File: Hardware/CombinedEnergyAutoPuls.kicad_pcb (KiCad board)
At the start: 2 copper layers, 0 parts

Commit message: STAGE: Component placed on PCB
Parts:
- added A1: Arduino_Ethernet, Local_MCU_Module_Library:Arduino_Ethernet_WithMountingHoles, F.Cu at (33.0, 2.54)
- added C1: C330nf, Capacitor_SMD:C_0805_2012Metric, F.Cu at (55.9, 62.2)
- added C2: C10uf, Capacitor_SMD:C_0603_1608Metric, F.Cu at (20.3, 63.5)
- added C3: C100nf, Capacitor_SMD:C_0402_1005Metric, F.Cu at (71.1, 61.0)
- added D1: 1N4148WS, Diode_SMD:D_SOD-323F, F.Cu at (55.9, 7.62)
- added D10: D_Z2V7, Diode_THT:D_DO-34_SOD68_P7.62mm_Horizontal, F.Cu at (68.6, 50.8)
- added D11: 1N4004, Diode_THT:D_DO-41_SOD81_P12.70mm_Horizontal, F.Cu at (55.9, 55.9)
- added D2: 1N4148WS, Diode_SMD:D_SOD-323F, F.Cu at (53.3, 7.62)
- added D3: 1N4148WS, Diode_SMD:D_SOD-323F, F.Cu at (50.8, 7.62)
- added D4: 1N4148WS, Diode_SMD:D_SOD-323F, F.Cu at (41.9, 44.5)
- added D5: 1N4148WS, Diode_SMD:D_SOD-323F, F.Cu at (45.7, 44.5)
- added D6: 1N4148WS, Diode_SMD:D_SOD-323F, F.Cu at (48.3, 44.5)
- added D7: 1N4148WS, Diode_SMD:D_SOD-323F, F.Cu at (50.8, 44.5)
- added D8: 1N4148WS, Diode_SMD:D_SOD-323F, F.Cu at (55.9, 44.5)
- added D9: LED_G3, LED_THT:LED_D3.0mm, F.Cu at (39.4, 57.3)
- added J1: Screw_Terminal_01x04, Local_Connectors:TerminalBlock_PT-1,5-4-5.0-H_1x04_P5.00mm_Horizontal-(F.Mount), F.Cu at (77.7, 41.0)
- added J2: Screw_Terminal_01x04, Local_Connectors:TerminalBlock_PT-1,5-4-5.0-H_1x04_P5.00mm_Horizontal-(F.Mount), F.Cu at (77.7, 20.7)
- added J3: Arduino_USB-Serial_Card, Local_Connectors:Arduino_USB-Serial_Card, F.Cu at (102.9, 2.54)
- added J4: Arduino_USB-Serial_Card_Connector, Local_Connectors:Arduino_USB-Serial_Card_EdgeConn, F.Cu at (34.6, 62.0)
- added J5: AudioJack3_Switch, Local_Connectors:AUDIO_JACK_ASJ-195-L-HT-(F.Mount), F.Cu at (0.10, 55.5)
- added J6: Screw_Terminal_01x04, Local_Connectors:TerminalBlock_PT-1,5-4-5.0-H_1x04_P5.00mm_Horizontal-(F.Mount), F.Cu at (77.7, 61.3)
- added JP1: Jumper_3_Bridged12, Connector_PinHeader_2.54mm:PinHeader_1x03_P2.54mm_Vertical, F.Cu at (15.2, 57.0)
- added Q1: S8550_PNP, Package_TO_SOT_SMD:SOT-23, F.Cu at (59.7, 14.0)
- added Q2: S8050_NPN, Package_TO_SOT_SMD:SOT-23, F.Cu at (62.2, 24.1)
- added Q3: S8050_NPN, Package_TO_SOT_SMD:SOT-23, F.Cu at (25.4, 62.2)
- added R1: R10K, Resistor_SMD:R_0402_1005Metric, F.Cu at (53.3, 15.2)
- added R2: R680K, Resistor_SMD:R_0603_1608Metric, F.Cu at (53.3, 12.7)
- added R3: R39K, Resistor_SMD:R_0402_1005Metric, F.Cu at (67.3, 24.9)
- added R4: R180K, Resistor_SMD:R_0603_1608Metric, F.Cu at (62.2, 19.1)
- added R5: R180K, Resistor_SMD:R_0603_1608Metric, F.Cu at (58.4, 7.62)
- added R6: R220, Resistor_SMD:R_0805_2012Metric, F.Cu at (49.5, 54.6)
- added R7: R56, Resistor_SMD:R_1206_3216Metric, F.Cu at (20.3, 59.7)
- added R8: R10K, Resistor_SMD:R_0402_1005Metric, F.Cu at (19.1, 55.9)
- added R9: R10K, Resistor_SMD:R_0402_1005Metric, F.Cu at (24.1, 55.9)
- added U1: L78S05CV, Package_TO_SOT_THT:TO-220-3_Vertical, F.Cu at (66.0, 61.3)
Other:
- board outline added: 113.8 x 67 mm

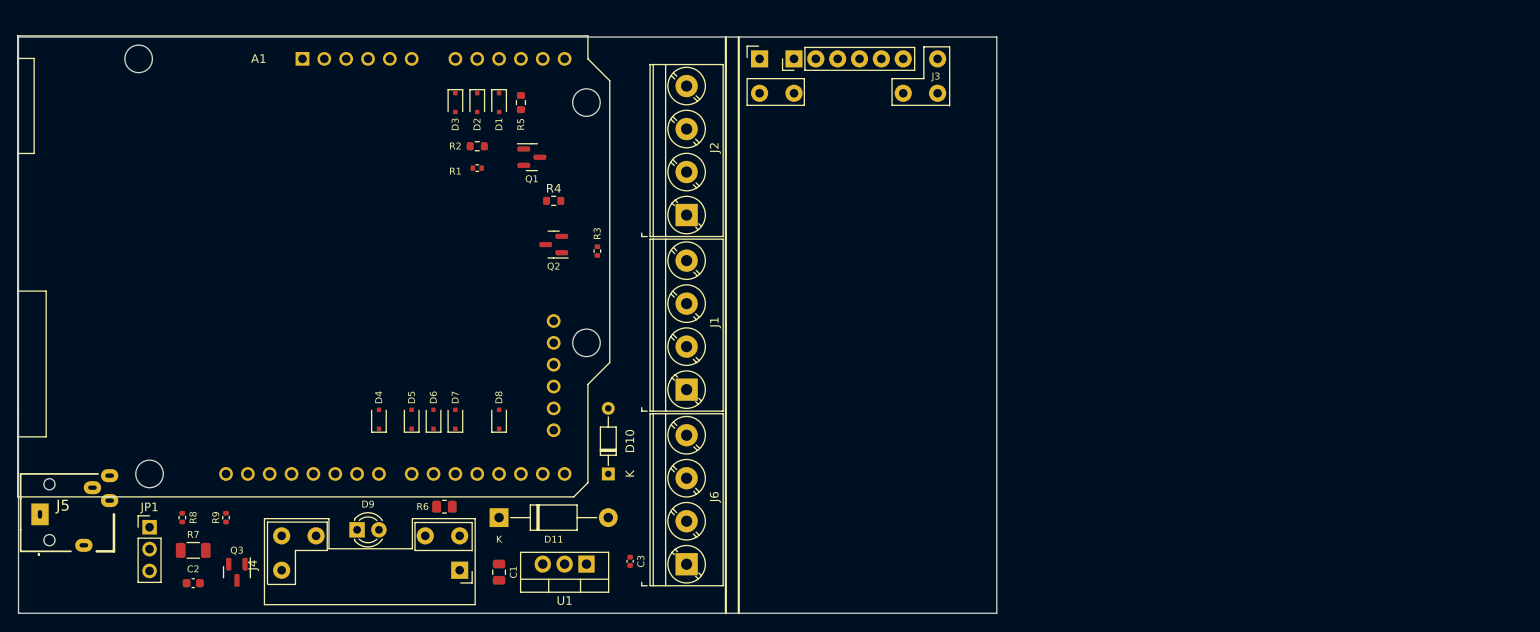
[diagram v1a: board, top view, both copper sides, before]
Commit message: Schematics and components placed on BCB for autoStart added to the project.
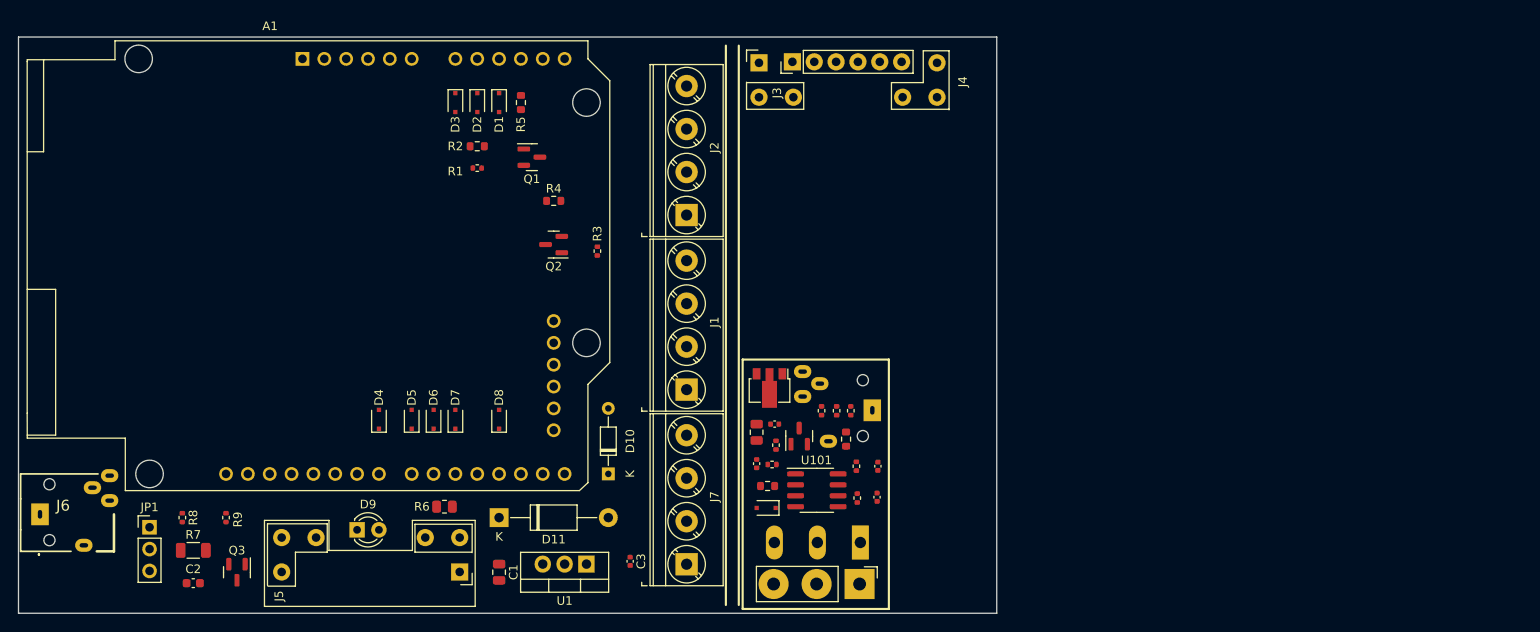
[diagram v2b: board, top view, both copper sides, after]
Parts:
- added C101: C10nf, Capacitor_SMD:C_0402_1005Metric, F.Cu at (99.9, 49.9)
- added C102: C100nf, Capacitor_SMD:C_0402_1005Metric, F.Cu at (99.8, 53.5)
- added C103: C100nf, Capacitor_SMD:C_0402_1005Metric, F.Cu at (85.8, 49.6)
- added C104: C100nf, Capacitor_SMD:C_0402_1005Metric, F.Cu at (87.9, 45.0)
- added C105: C330nf, Capacitor_SMD:C_0805_2012Metric, F.Cu at (85.8, 46.0)
- added D101: 1N4148WS, Diode_SMD:D_SOD-323F, F.Cu at (86.9, 54.8)
- added J101: AudioJack3_Switch, Local_Connectors:AUDIO_JACK_ASJ-195-L-HT-(B.Mount), F.Cu at (101.7, 43.4)
- added J102: Screw_Terminal_01x03, Local_Connectors:Phoenix_TERM_BLOCK_3POS_45DEG_5MM_PCB-(B.Mount), F.Cu at (97.9, 58.8)
- added J103: Conn_3P, Local_Connectors:PinHeader_1x03_P_5mm_Vertical-(F.Mount), F.Cu at (97.8, 63.6)
- added J5: Arduino_USB-Serial_Card_Connector, Local_Connectors:Arduino_USB-Serial_Card_EdgeConn, F.Cu at (34.6, 62.2)
- added Q101: S8050, Package_TO_SOT_SMD:SOT-23, F.Cu at (90.8, 46.4)
- added R101: R10K, Resistor_SMD:R_0402_1005Metric, F.Cu at (96.8, 43.5)
- added R102: R10K, Resistor_SMD:R_0402_1005Metric, F.Cu at (95.1, 43.5)
- added R103: R10K, Resistor_SMD:R_0402_1005Metric, F.Cu at (93.4, 43.5)
- added R104: R330K, Resistor_SMD:R_0402_1005Metric, F.Cu at (97.4, 49.9)
- added R105: R100K, Resistor_SMD:R_0402_1005Metric, F.Cu at (97.5, 53.6)
- added R106: R680K, Resistor_SMD:R_0603_1608Metric, F.Cu at (87.1, 52.2)
- added R107: R150K, Resistor_SMD:R_0402_1005Metric, F.Cu at (88.1, 47.5)
- added R108: R33K, Resistor_SMD:R_0402_1005Metric, F.Cu at (87.6, 49.7)
- added R109: R180K, Resistor_SMD:R_0603_1608Metric, F.Cu at (96.2, 46.8)
- added U101: LM358DR2G, Package_SO:SOIC-8_3.9x4.9mm_P1.27mm, F.Cu at (92.8, 52.7)
- added U102: 78L05, Package_TO_SOT_SMD:SOT-89-3, F.Cu at (87.3, 40.8)
- J3: value Arduino_USB-Serial_Card -> Pin_Header_1x6; footprint Local_Connectors:Arduino_USB-Serial_Card -> Local_Connectors:PinHeader_1x06_P_0,1in_Vertical
- J4: value Arduino_USB-Serial_Card_Connector -> Arduino_USB-Serial_Card; footprint Local_Connectors:Arduino_USB-Serial_Card_EdgeConn -> Local_Connectors:Arduino_USB-Serial_Card
- moved J4 78.3 mm to (86.1, 3.00), turned to -90 degrees
- moved J3 12.9 mm to (90.0, 2.88), turned to 90 degrees
- renumbered J5 to J6, J6 to J7
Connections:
- J3 pad 1: unconnected-(J3-Pad1) -> GND3
- J3 pad 2: unconnected-(J3-Pad2) -> Net-(J3-Pad2)
- J3 pad 3: unconnected-(J3-Pad3) -> VCC1
- J3 pad 4: unconnected-(J3-Pad4) -> Net-(J3-Pad4)
- J3 pad 5: unconnected-(J3-Pad5) -> Net-(J3-Pad5)
- J3 pad 6: unconnected-(J3-Pad6) -> Net-(J3-Pad6)
- J4 pad 1: GND -> GND3
- J4 pad 2: Net-(A1-Pad30) -> Net-(J3-Pad2)
- J4 pad 3: VCC -> VCC1
- J4 pad 4: Net-(A1-Pad32) -> Net-(J3-Pad4)
- J4 pad 5: Net-(A1-Pad33) -> Net-(J3-Pad5)
- J4 pad 6: Net-(A1-Pad34) -> Net-(J3-Pad6)

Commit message: UPD: - Schematics and components placed on BCB for ProgrameablePulseGenerator added to the project
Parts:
- added A201: Arduino_Nano_v3, Module:Arduino_Nano, F.Cu at (122.7, 43.0)
- added AE201: Antenna, Local_Misckllaneous_Library:Undefined_Antenna(B.Mount), F.Cu at (111.8, 4.45)
- added C201: C100nf, Capacitor_SMD:C_0402_1005Metric, F.Cu at (129.5, 63.0)
- added C202: C330nf, Capacitor_SMD:C_0805_2012Metric, F.Cu at (129.5, 58.4)
- added D201: 1N4148WS, Diode_SMD:D_SOD-323F, F.Cu at (163.2, 50.8)
- added D202: LED, LED_SMD:LED_0805_2012Metric, F.Cu at (128.8, 53.3)
- added D203: 1N4148WS, Diode_SMD:D_SOD-323F, F.Cu at (163.2, 45.7)
- added D204: LED, LED_SMD:LED_0805_2012Metric, F.Cu at (128.6, 48.3)
- added D205: 1N4148WS, Diode_SMD:D_SOD-323F, F.Cu at (163.2, 40.6)
- added D206: LED, LED_SMD:LED_0805_2012Metric, F.Cu at (128.6, 43.2)
- added D207: 1N4148WS, Diode_SMD:D_SOD-323F, F.Cu at (163.2, 35.6)
- added D208: LED, LED_SMD:LED_0805_2012Metric, F.Cu at (128.6, 38.1)
- added D209: 1N4148WS, Diode_SMD:D_SOD-323F, F.Cu at (163.2, 30.5)
- added D210: LED, LED_SMD:LED_0805_2012Metric, F.Cu at (128.6, 33.0)
- added D211: 1N4148WS, Diode_SMD:D_SOD-323F, F.Cu at (163.2, 25.4)
- added D212: LED, LED_SMD:LED_0805_2012Metric, F.Cu at (128.6, 27.9)
- added D213: 1N4148WS, Diode_SMD:D_SOD-323F, F.Cu at (163.2, 20.3)
- added D214: LED, LED_SMD:LED_0805_2012Metric, F.Cu at (128.8, 22.9)
- added D215: 1N4148WS, Diode_SMD:D_SOD-323F, F.Cu at (163.2, 15.2)
- added D216: LED, LED_SMD:LED_0805_2012Metric, F.Cu at (128.8, 17.8)
- added D217: 1N4148WS, Diode_SMD:D_SOD-323F, F.Cu at (163.2, 10.2)
- added D218: LED, LED_SMD:LED_0805_2012Metric, F.Cu at (128.8, 12.7)
- added D219: 1N4148WS, Diode_SMD:D_SOD-323F, F.Cu at (163.2, 5.08)
- added D220: LED, LED_SMD:LED_0805_2012Metric, F.Cu at (128.8, 7.62)
- added J201: Conn_20P_Female, Connector_PinHeader_2.54mm:PinHeader_1x20_P2.54mm_Vertical, F.Cu at (142.2, 53.3)
- added J202: Conn_20P_Female, Connector_PinHeader_2.54mm:PinHeader_1x20_P2.54mm_Vertical, F.Cu at (170.2, 53.3)
- added J203: Conn_4P_Female, Connector_PinHeader_2.54mm:PinHeader_1x04_P2.54mm_Vertical, F.Cu at (170.2, 63.5)
- added J204: Conn_4P_Female, Connector_PinHeader_2.54mm:PinHeader_1x04_P2.54mm_Vertical, F.Cu at (152.4, 63.5)
- added J205: Barrel_Jack_Switch, Local_Connectors:BarrelJack_Horizontal(F.Mount), F.Cu at (110.2, 52.4)
- added JP201: SolderJumper, Local_Connectors:SolderJumper-2_P1.3mm_Bridged_RoundedPad1.0x1.5mm(B.Mount), F.Cu at (163.2, 50.8)
- added JP202: SolderJumper, Local_Connectors:SolderJumper-2_P1.3mm_Bridged_RoundedPad1.0x1.5mm(B.Mount), F.Cu at (163.2, 45.7)
- added JP203: SolderJumper, Local_Connectors:SolderJumper-2_P1.3mm_Bridged_RoundedPad1.0x1.5mm(B.Mount), F.Cu at (163.2, 40.6)
- added JP204: SolderJumper, Local_Connectors:SolderJumper-2_P1.3mm_Bridged_RoundedPad1.0x1.5mm(B.Mount), F.Cu at (163.2, 35.6)
- added JP205: SolderJumper, Local_Connectors:SolderJumper-2_P1.3mm_Bridged_RoundedPad1.0x1.5mm(B.Mount), F.Cu at (163.2, 30.5)
- added JP206: SolderJumper, Local_Connectors:SolderJumper-2_P1.3mm_Bridged_RoundedPad1.0x1.5mm(B.Mount), F.Cu at (163.2, 25.4)
- added JP207: SolderJumper, Local_Connectors:SolderJumper-2_P1.3mm_Bridged_RoundedPad1.0x1.5mm(B.Mount), F.Cu at (163.2, 20.3)
- added JP208: SolderJumper, Local_Connectors:SolderJumper-2_P1.3mm_Bridged_RoundedPad1.0x1.5mm(B.Mount), F.Cu at (163.2, 15.2)
- added JP209: SolderJumper, Local_Connectors:SolderJumper-2_P1.3mm_Bridged_RoundedPad1.0x1.5mm(B.Mount), F.Cu at (163.2, 10.2)
- added JP210: SolderJumper, Local_Connectors:SolderJumper-2_P1.3mm_Bridged_RoundedPad1.0x1.5mm(B.Mount), F.Cu at (163.2, 5.08)
- added JP211: Jumper_3_Bridged12, Connector_PinHeader_2.54mm:PinHeader_1x03_P2.54mm_Vertical, F.Cu at (134.6, 58.4)
- added R201: R390, Resistor_SMD:R_0603_1608Metric, F.Cu at (135.5, 50.8)
- added R202: R180, Resistor_SMD:R_0805_2012Metric, F.Cu at (135.5, 53.3)
- added R203: R390, Resistor_SMD:R_0603_1608Metric, F.Cu at (135.4, 45.7)
- added R204: R180, Resistor_SMD:R_0805_2012Metric, F.Cu at (135.5, 48.3)
- added R205: R390, Resistor_SMD:R_0603_1608Metric, F.Cu at (135.4, 40.6)
- added R206: R180, Resistor_SMD:R_0805_2012Metric, F.Cu at (135.4, 43.2)
- added R207: R390, Resistor_SMD:R_0603_1608Metric, F.Cu at (135.4, 35.6)
- added R208: R180, Resistor_SMD:R_0805_2012Metric, F.Cu at (135.5, 38.1)
- added R209: R390, Resistor_SMD:R_0603_1608Metric, F.Cu at (135.4, 30.5)
- added R210: R180, Resistor_SMD:R_0805_2012Metric, F.Cu at (135.5, 33.0)
- added R211: R390, Resistor_SMD:R_0603_1608Metric, F.Cu at (135.4, 25.4)
- added R212: R180, Resistor_SMD:R_0805_2012Metric, F.Cu at (135.5, 27.9)
- added R213: R390, Resistor_SMD:R_0603_1608Metric, F.Cu at (135.4, 20.3)
- added R214: R180, Resistor_SMD:R_0805_2012Metric, F.Cu at (135.4, 22.9)
- added R215: R390, Resistor_SMD:R_0603_1608Metric, F.Cu at (135.5, 15.2)
- added R216: R180, Resistor_SMD:R_0805_2012Metric, F.Cu at (135.5, 17.8)
- added R217: R390, Resistor_SMD:R_0603_1608Metric, F.Cu at (135.5, 10.2)
- added R218: R180, Resistor_SMD:R_0805_2012Metric, F.Cu at (135.5, 12.7)
- added R219: R390, Resistor_SMD:R_0603_1608Metric, F.Cu at (135.4, 5.08)
- added R220: R180, Resistor_SMD:R_0805_2012Metric, F.Cu at (135.5, 7.62)
- added R221: R390, Resistor_SMD:R_0603_1608Metric, F.Cu at (144.8, 57.1)
- added SW201: THT_SW_4_Tactile, Local_Misckllaneous_Library:THT_SW_Tactile(F.Mount), F.Cu at (118.3, 58.7)
- added U201: PC817, Local_Misckllaneous_Library:DIP-4_W7.62mm_Slim(F.Mount), F.Cu at (148.6, 50.8)
- added U202: PC817, Local_Misckllaneous_Library:DIP-4_W7.62mm_Slim(F.Mount), F.Cu at (148.6, 45.7)
- added U203: PC817, Local_Misckllaneous_Library:DIP-4_W7.62mm_Slim(F.Mount), F.Cu at (148.6, 40.6)
- added U204: PC817, Local_Misckllaneous_Library:DIP-4_W7.62mm_Slim(F.Mount), F.Cu at (148.6, 35.6)
- added U205: PC817, Local_Misckllaneous_Library:DIP-4_W7.62mm_Slim(F.Mount), F.Cu at (148.6, 30.5)
- added U206: PC817, Local_Misckllaneous_Library:DIP-4_W7.62mm_Slim(F.Mount), F.Cu at (148.6, 25.4)
- added U207: PC817, Local_Misckllaneous_Library:DIP-4_W7.62mm_Slim(F.Mount), F.Cu at (148.6, 20.3)
- added U208: PC817, Local_Misckllaneous_Library:DIP-4_W7.62mm_Slim(F.Mount), F.Cu at (148.6, 15.2)
- added U209: PC817, Local_Misckllaneous_Library:DIP-4_W7.62mm_Slim(F.Mount), F.Cu at (148.5, 10.2)
- added U210: PC817, Local_Misckllaneous_Library:DIP-4_W7.62mm_Slim(F.Mount), F.Cu at (148.5, 5.00)
- added U211: PC817, Local_Misckllaneous_Library:DIP-4_W7.62mm_Slim(F.Mount), F.Cu at (148.6, 55.9)
- added U212: L78S05CV, Package_TO_SOT_THT:TO-220-3_Vertical, F.Cu at (118.7, 51.5)
- D10: value D_Z2V7 -> D_Z2V4; footprint Diode_THT:D_DO-34_SOD68_P7.62mm_Horizontal -> Diode_THT:D_DO-35_SOD27_P7.62mm_Horizontal
- J4: value Arduino_USB-Serial_Card -> Arduino_USB-Serial_Card_Connector
- J5: value Arduino_USB-Serial_Card_Connector -> Arduino_USB-Serial_Edge_Connector
- Q101: value S8050 -> S8050_NPN
- moved J4 5.20 mm to (91.3, 2.80), turned to 180 degrees
- moved J3 4.11 mm to (91.4, 6.74), turned to 0 degrees
- moved J101 1.31 mm to (102.2, 42.2)
- moved C101 1.08 mm to (100.8, 49.3)
- moved J103 1.08 mm to (98.7, 63.0)
- moved R102 1.08 mm to (96.0, 42.9)
- moved R103 1.08 mm to (94.3, 42.9)
- moved R104 1.08 mm to (98.3, 49.3)
- moved R106 1.08 mm to (88.0, 51.6)
- moved R108 1.08 mm to (88.5, 49.1)
- moved C104 1.08 mm to (88.8, 44.4)
- moved D101 1.08 mm to (87.8, 54.2)
- moved R109 1.08 mm to (97.1, 46.2)
- moved C103 1.08 mm to (86.7, 49.0)
- moved C105 1.08 mm to (86.7, 45.4)
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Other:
- board size 113.8 x 67 mm -> 174.9 x 67 mm
- board text added: "OC 5V Vin GND"
- board text added: "Open Collector Output D 2-11"
- board text added: "Output D 2-11"

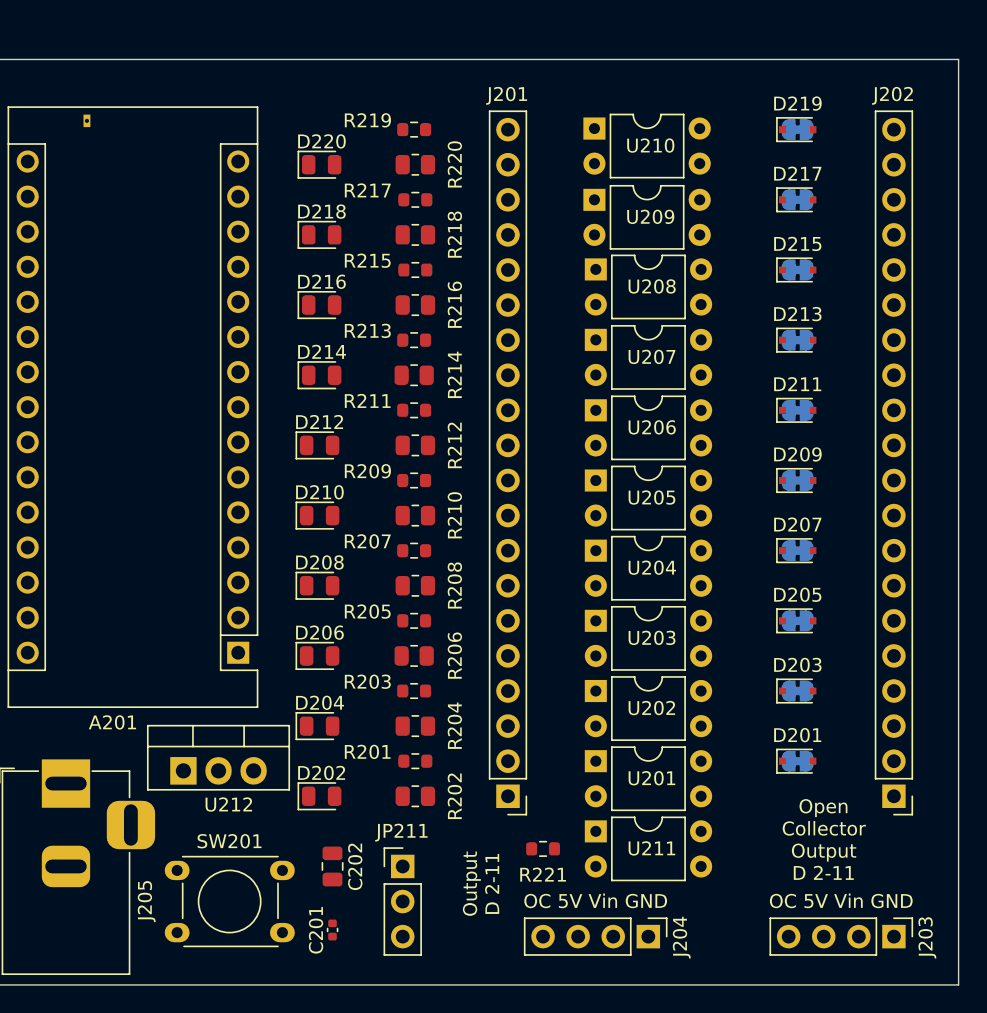
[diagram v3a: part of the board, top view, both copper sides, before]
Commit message: UPD: Silkmask references modified
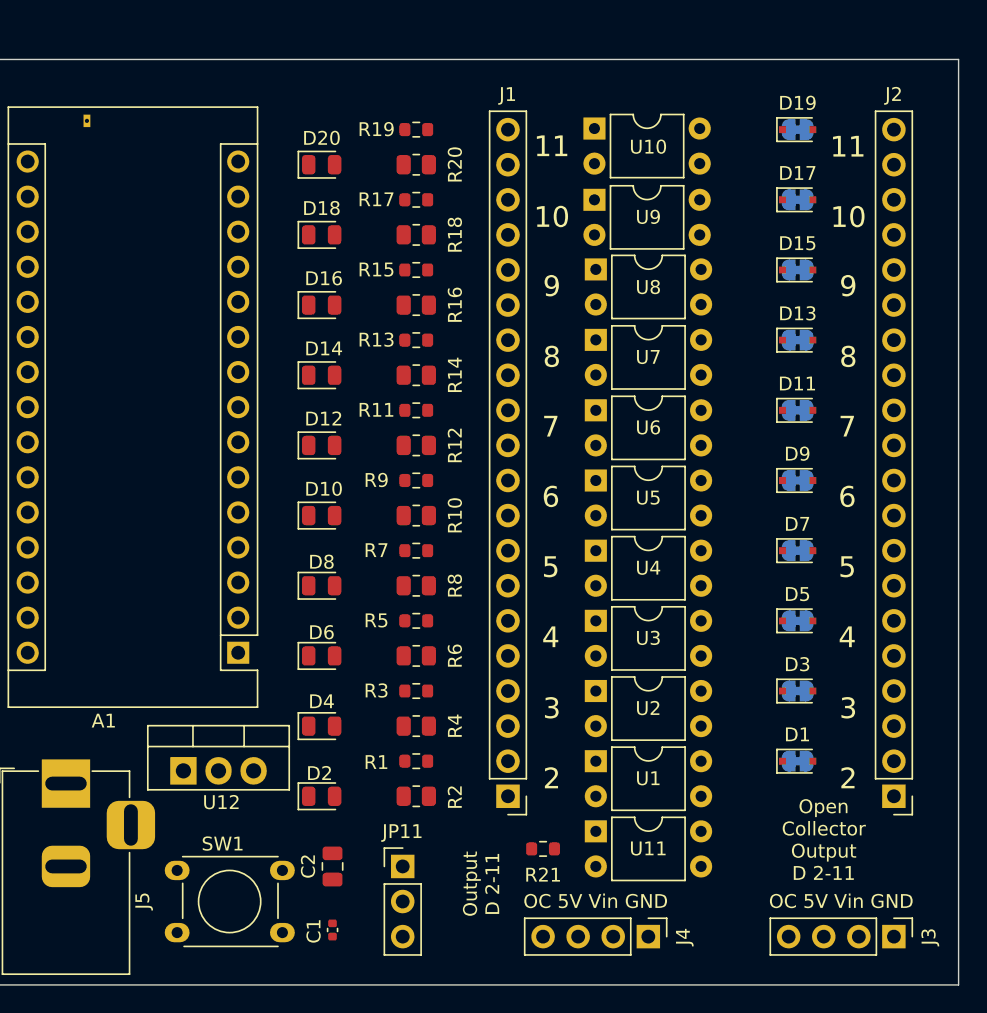
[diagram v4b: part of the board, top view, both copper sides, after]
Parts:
- moved R203 0.16 mm to (135.6, 45.7)
- moved R205 0.16 mm to (135.6, 40.6)
- moved R207 0.16 mm to (135.6, 35.6)
- moved R209 0.16 mm to (135.6, 30.5)
- moved R211 0.16 mm to (135.6, 25.4)
- moved R213 0.16 mm to (135.6, 20.3)
- moved R214 0.16 mm to (135.6, 22.9), turned to 180 degrees
- moved R219 0.16 mm to (135.6, 5.08)
- moved Rw 0.16 mm to (135.6, 43.2), turned to 180 degrees
- moved D204 0.15 mm to (128.8, 48.3)
- moved D206 0.15 mm to (128.8, 43.2)
- moved D208 0.15 mm to (128.8, 38.1)
- moved D210 0.15 mm to (128.8, 33.0)
- moved D212 0.15 mm to (128.8, 27.9)
- moved R201 0.07 mm to (135.6, 50.8)
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- renumbered R206 to Rw, R202 to R½
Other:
- board text added: "10"
- board text added: "11"
- board text added: "2"
- board text added: "3"
- board text added: "4"
- board text added: "5"
- board text added: "6"
- board text added: "7"
- board text added: "8"
- board text added: "9"

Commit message: UPD  - Adding critical traces by hand and prepare for autorouter to do the rest.
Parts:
- turned D201 to 180 degrees
- turned D203 to 180 degrees
- turned D205 to 180 degrees
- turned D207 to 180 degrees
- turned D209 to 180 degrees
- turned D211 to 180 degrees
- turned D213 to 180 degrees
- turned D215 to 180 degrees
- turned D217 to 180 degrees
- turned D219 to 180 degrees
- renumbered R½ to R202, Rw to R206
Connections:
- J203 pad 3: Net-(J203-Pad3) -> /Arduino_5V
- J204 pad 3: Net-(J203-Pad3) -> /Arduino_5V
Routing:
- net GND4: track 0.00 -> 215.0 mm, vias 0 -> 1
- net /Arduino_5V: track 0.00 -> 145.1 mm, vias 0 -> 10
- net GND: track 0.00 -> 108.0 mm, vias 0 -> 3
- net Net-(A1-Pad6): track 0.00 -> 72.8 mm
- net Net-(JP211-Pad2): track 0.00 -> 67.5 mm, vias 0 -> 10
- net Vin: track 0.00 -> 66.9 mm
- net Net-(A201-Pad5): track 0.00 -> 46.9 mm
- net Net-(D201-Pad2): track 0.00 -> 45.7 mm
- net Net-(A201-Pad6): track 0.00 -> 44.3 mm
- net Net-(A201-Pad7): track 0.00 -> 41.8 mm
- net Net-(A201-Pad8): track 0.00 -> 39.3 mm
- net Net-(A201-Pad9): track 0.00 -> 37.2 mm
- net Net-(A201-Pad10): track 0.00 -> 34.2 mm
- net Net-(A201-Pad11): track 0.00 -> 31.6 mm
- net Net-(A201-Pad12): track 0.00 -> 30.5 mm
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- added copper zone on B.Cu, net Net-(A201-Pad19)
